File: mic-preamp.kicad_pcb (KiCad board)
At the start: 2 copper layers, 41.6 x 56.6 mm, 33 parts, among them P1 CONN_4, U1 MCP6234-E/SL, U2 LM339

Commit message: Routed and generated gerber
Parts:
- added C4: 47u, visgence_parts:SM1206POL_VIS, F.Cu at (78.5, 59.2)
- added G***: LOGO, visgence_parts:LOGO, F.Cu at (56.0, 88.0)
- added G***: LOGO, visgence_parts:LOGOMIRROR, B.Cu at (67.0, 76.0)
- moved R1 31.6 mm to (82.5, 57.2), turned to 270 degrees
- moved D1 28.1 mm to (82.5, 61.2), turned to 270 degrees
- moved R3 13.6 mm to (52.0, 62.0)
- moved R4 13.6 mm to (52.0, 66.0)
- moved R2 13.6 mm to (52.0, 58.0), turned to 270 degrees
- moved R5 13.5 mm to (52.0, 70.0)
- moved R6 13.5 mm to (52.0, 74.0)
- moved U1 12.0 mm to (67.5, 80.0)
- moved R16 11.9 mm to (67.5, 87.2)
- moved C1 11.2 mm to (58.2, 76.0), turned to 270 degrees
- moved RV1 10.9 mm to (80.5, 87.8)
- moved U2 9.65 mm to (67.5, 64.5), turned to 0 degrees
- moved R9 9.53 mm to (61.2, 76.0), turned to 90 degrees
- moved C3 8.95 mm to (58.2, 83.0), turned to 270 degrees
- moved R11 7.97 mm to (61.2, 83.0), turned to 90 degrees
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- gave numbers to parts that had none: 4
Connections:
- P1 pad 1: GND -> out
- P1 pad 2: +5V -> Net-(P1-Pad2)
- P1 pad 3: Net-(P1-Pad3) -> +5V
- P1 pad 4: out -> GND
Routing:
- net +5V: track 0.00 -> 138.6 mm, vias 0 -> 1
- net GND: track 0.00 -> 130.7 mm, vias 0 -> 2
- net out: track 0.00 -> 48.0 mm
- net Net-(C3-Pad1): track 0.00 -> 46.3 mm
- net Net-(U1-Pad13): track 0.00 -> 27.7 mm
- net Net-(R4-Pad2): track 0.00 -> 23.7 mm
- net Net-(R2-Pad2): track 0.00 -> 22.5 mm
- net Net-(R5-Pad2): track 0.00 -> 22.2 mm
- net Net-(D5-Pad2): track 0.00 -> 20.5 mm, vias 0 -> 2
- net Net-(D4-Pad2): track 0.00 -> 19.4 mm, vias 0 -> 2
- net Net-(R3-Pad2): track 0.00 -> 19.4 mm
- net Net-(D2-Pad2): track 0.00 -> 19.3 mm, vias 0 -> 2
- net Net-(D3-Pad2): track 0.00 -> 19.0 mm, vias 0 -> 2
- net Net-(R16-Pad1): track 0.00 -> 18.3 mm
- net vhalf: track 0.00 -> 11.4 mm
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- added copper zone on B.Cu, net GND
- added copper zone on F.Cu, net GND
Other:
- net class Default: trace_width 0.254 -> 0.508
- board text added: "2014 Visgence Inc."
- board text added: "GND"
- board text added: "Microphone Preamp"
- board text added: "N/C"
- board text added: "OUT"
- board text added: "VCC"

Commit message: Fixed solder mask
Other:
- rule pad_to_mask_clearance: 0.2 -> 0
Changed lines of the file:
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@@
     (pad_size 1.524 1.524)
     (pad_drill 0.762)
-    (pad_to_mask_clearance 0.2)
+    (pad_to_mask_clearance 0)
     (aux_axis_origin 0 0)
     (visible_elements 7FFFF77F)

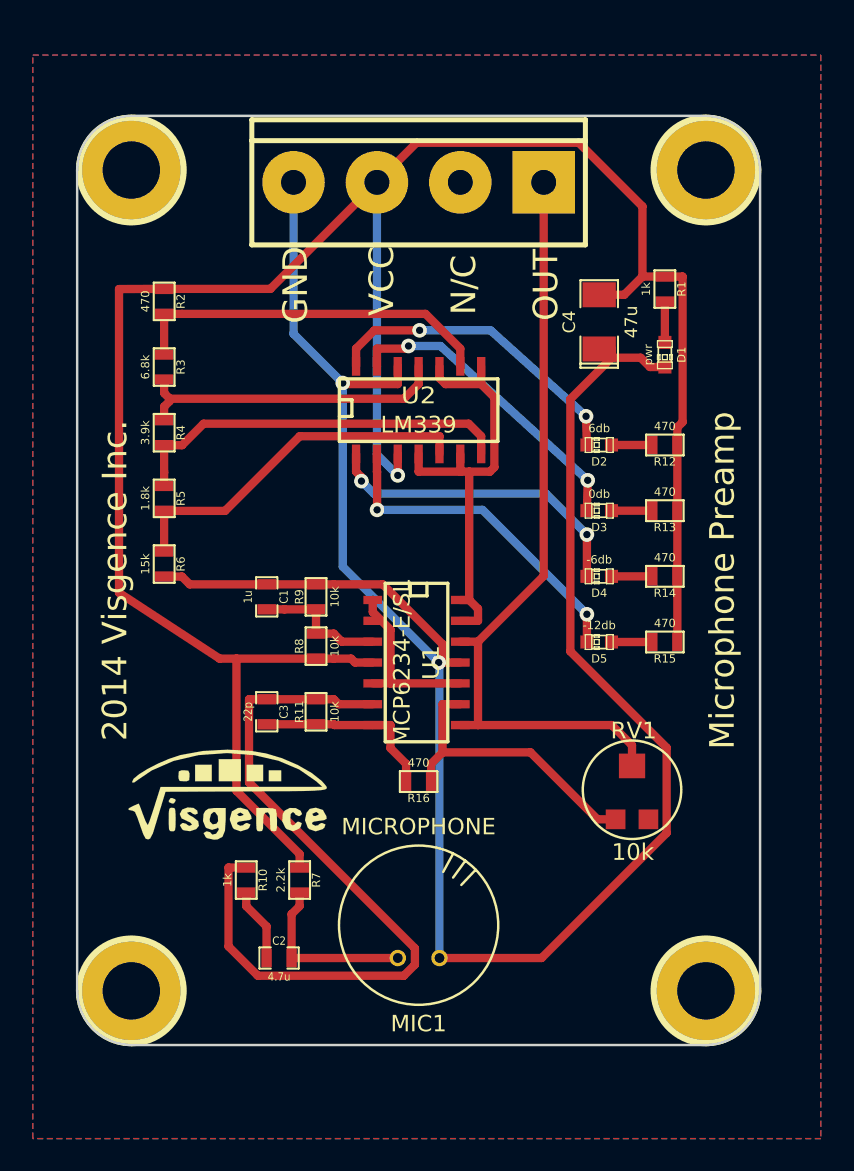
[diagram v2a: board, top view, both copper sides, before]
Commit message: resized board, change gain
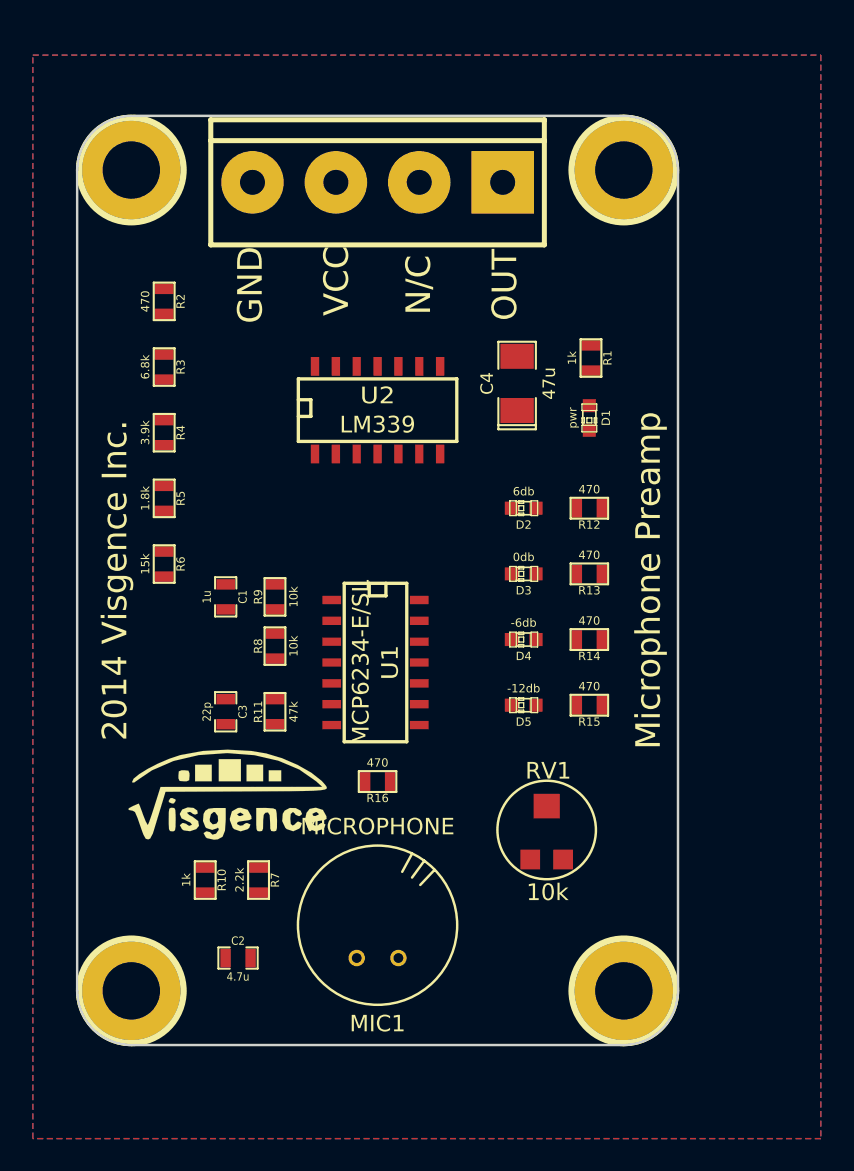
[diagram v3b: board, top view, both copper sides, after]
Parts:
- R11: value 10k -> 47k
- moved C4 6.25 mm to (73.5, 63.0)
- moved R1 6.16 mm to (78.0, 61.5)
- moved D1 6.00 mm to (77.9, 65.1)
- moved D2 6.00 mm to (73.9, 70.6)
- moved D3 6.00 mm to (73.9, 74.6)
- moved D4 6.00 mm to (73.9, 78.6)
- moved D5 6.00 mm to (73.9, 82.6)
- moved R12 6.00 mm to (77.9, 70.6)
- moved R13 6.00 mm to (77.9, 74.6)
- moved R14 6.00 mm to (77.9, 78.6)
- moved R15 6.00 mm to (77.9, 82.6)
- moved RV1 5.75 mm to (75.3, 90.2)
- moved h2 5.00 mm to (80.0, 50.0)
- moved h4 5.00 mm to (80.0, 100.0)
- moved C1 2.50 mm to (55.8, 76.0)
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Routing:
- net +5V: track 138.6 -> 0.00 mm, vias 1 -> 0
- net GND: track 130.7 -> 0.00 mm, vias 2 -> 0
- net out: track 48.0 -> 0.00 mm
- net Net-(C3-Pad1): track 46.3 -> 0.00 mm
- net Net-(U1-Pad13): track 27.7 -> 0.00 mm
- net Net-(R4-Pad2): track 23.7 -> 0.00 mm
- net Net-(R2-Pad2): track 22.5 -> 0.00 mm
- net Net-(R5-Pad2): track 22.2 -> 0.00 mm
- net Net-(D5-Pad2): track 20.5 -> 0.00 mm, vias 2 -> 0
- net Net-(D4-Pad2): track 19.4 -> 0.00 mm, vias 2 -> 0
- net Net-(R3-Pad2): track 19.4 -> 0.00 mm
- net Net-(D2-Pad2): track 19.3 -> 0.00 mm, vias 2 -> 0
- net Net-(D3-Pad2): track 19.0 -> 0.00 mm, vias 2 -> 0
- net Net-(R16-Pad1): track 18.3 -> 0.00 mm
- net vhalf: track 11.4 -> 0.00 mm
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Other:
- board size 41.6 x 56.6 mm -> 36.6 x 56.6 mm

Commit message: re-routed board
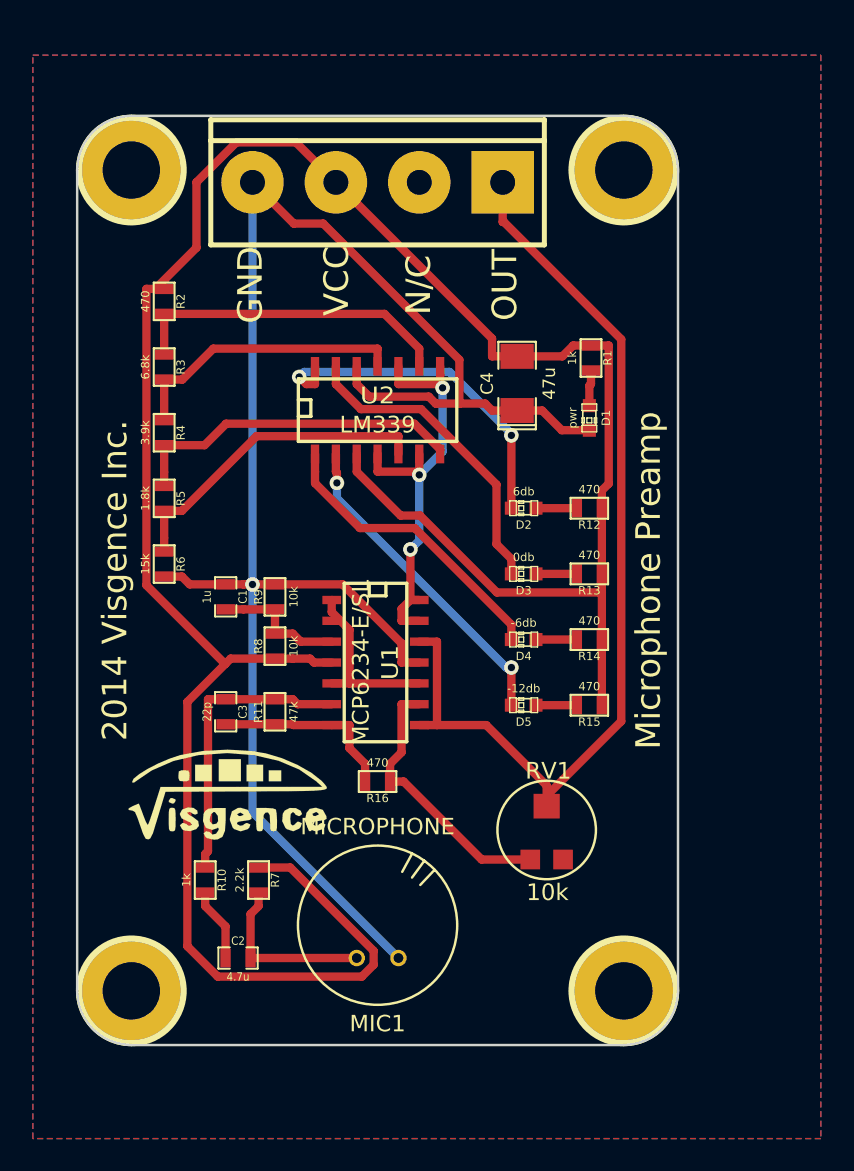
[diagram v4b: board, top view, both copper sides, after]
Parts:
- renumbered G*** to G1
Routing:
- net +5V: track 0.00 -> 154.3 mm
- net GND: track 0.00 -> 105.5 mm, vias 0 -> 1
- net out: track 0.00 -> 59.0 mm
- net Net-(U1-Pad13): track 0.00 -> 26.7 mm, vias 0 -> 3
- net Net-(D2-Pad2): track 0.00 -> 21.4 mm, vias 0 -> 2
- net Net-(R4-Pad2): track 0.00 -> 20.8 mm
- net Net-(R2-Pad2): track 0.00 -> 20.0 mm
- net Net-(D5-Pad2): track 0.00 -> 19.9 mm, vias 0 -> 2
- net Net-(R5-Pad2): track 0.00 -> 19.7 mm
- net Net-(D3-Pad2): track 0.00 -> 19.2 mm
- net Net-(D4-Pad2): track 0.00 -> 18.2 mm
- net Net-(C3-Pad1): track 0.00 -> 18.0 mm
- net Net-(R3-Pad2): track 0.00 -> 17.3 mm
- net Net-(R16-Pad1): track 0.00 -> 16.6 mm
- net vhalf: track 0.00 -> 11.4 mm
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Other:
- outline, holes or cut-outs redrawn
